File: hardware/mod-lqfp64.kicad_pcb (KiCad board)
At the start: 2 copper layers, 25.1 x 27.9 mm, 13 parts, among them J1 Target, J2 Target_HS, U1 STM32F405RGTx, Y1 8MHz

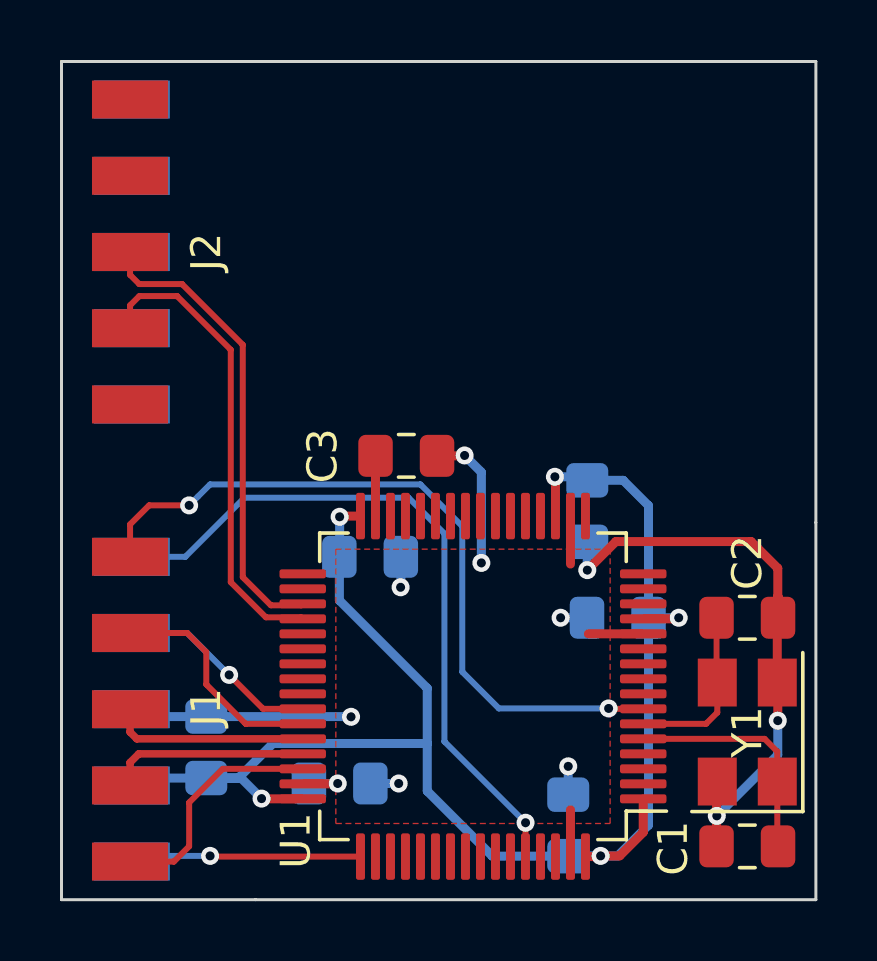
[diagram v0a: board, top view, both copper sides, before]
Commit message: Update mod-lqfp64 board layout
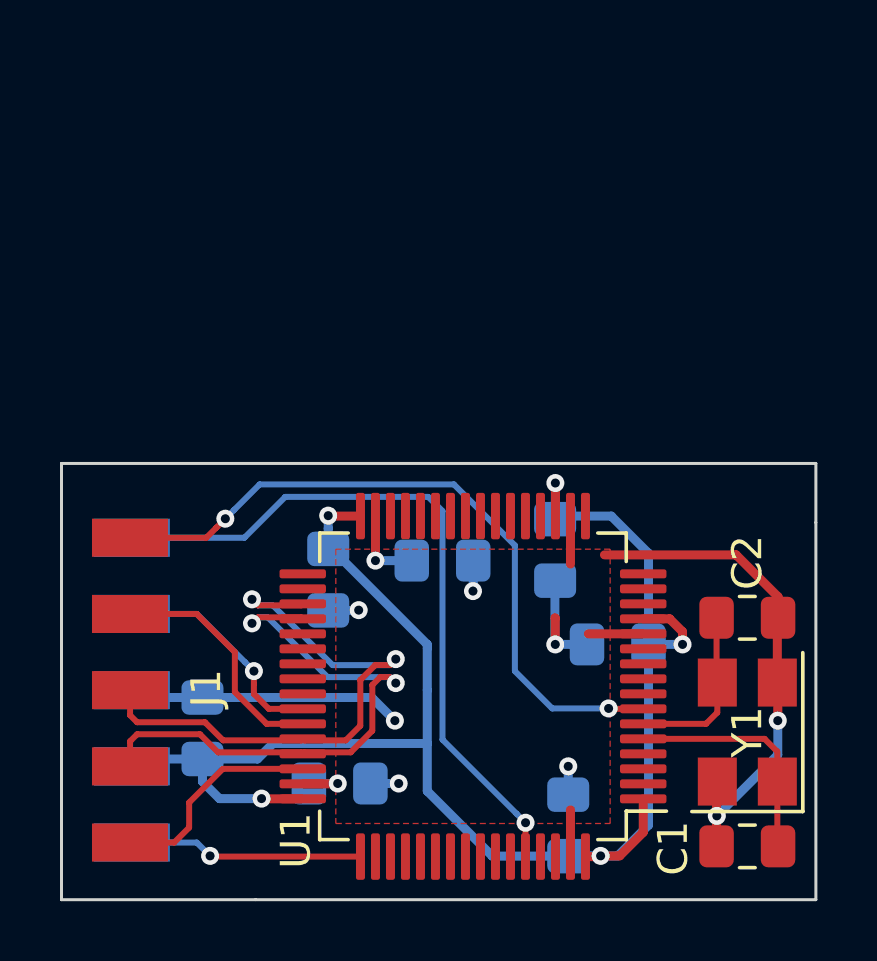
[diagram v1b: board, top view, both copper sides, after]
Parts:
- removed J2: Target_HS, unsorted:BH-10-Edge
- C3: moved to B.Cu
- moved C3 3.70 mm to (44.7, 45.2)
- moved C9 1.68 mm to (48.5, 44.9)
- moved C5 1.59 mm to (40.9, 45.8), turned to 270 degrees
- moved C6 0.89 mm to (50.5, 48.0)
- moved C7 0.65 mm to (36.7, 50.8)
- moved J1 0.63 mm to (34.3, 49.5)
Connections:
- U1 pad 35: /HUSB_D- -> /USB_D-
- U1 pad 36: /HUSB_D+ -> /USB_D+
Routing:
- net /HUSB_D-: track 15.6 -> 0.00 mm
- net /HUSB_D+: track 15.6 -> 0.00 mm
- net /USB_D-: track 6.61 -> 19.7 mm, vias 0 -> 2
- net /USB_D+: track 6.64 -> 19.7 mm, vias 0 -> 2
- net +3V3: track 54.8 -> 56.6 mm
- net GND: track 40.3 -> 38.9 mm, vias 10 -> 8
- net /NRST: track 24.7 -> 23.4 mm
- net /TX: track 6.75 -> 7.46 mm
- net /VCAP_1: track 2.01 -> 2.69 mm, vias 0 -> 1
- net /SWDIO: track 7.89 -> 7.26 mm
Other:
- board size 25.1 x 27.9 mm -> 25.1 x 14.5 mm
